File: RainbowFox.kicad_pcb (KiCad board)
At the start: 2 copper layers, 304.8 x 95.3 mm, 315 parts, among them P1 FLASH_HDR, P2 CONN_01X06, P3 USB_OTG, P4 CONN_01X04, U1 MK20DX256VLH7, U2 IS31FL3737, U3 IS31FL3737, X1 CRYSTAL_SMD

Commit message: Fixed Orientation of Keyboard-Diodes
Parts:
- turned D1 to 180 degrees
- turned D10 to 90 degrees
- turned D11 to 90 degrees
- turned D12 to 90 degrees
- turned D13 to 90 degrees
- turned D14 to 90 degrees
- turned D15 to 90 degrees
- turned D16 to 0 degrees
- turned D17 to 90 degrees
- turned D18 to 90 degrees
- turned D19 to 90 degrees
- turned D2 to 0 degrees
- turned D20 to 90 degrees
- turned D21 to 90 degrees
- turned D22 to 90 degrees
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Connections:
- D1 pad 1: Net-(D1-Pad1) -> /mcu/PTB19
- D1 pad 2: /mcu/PTB19 -> Net-(D1-Pad2)
- D10 pad 1: Net-(D10-Pad1) -> /mcu/PTB19
- D10 pad 2: /mcu/PTB19 -> Net-(D10-Pad2)
- D11 pad 1: Net-(D11-Pad1) -> /mcu/PTB19
- D11 pad 2: /mcu/PTB19 -> Net-(D11-Pad2)
- D12 pad 1: Net-(D12-Pad1) -> /mcu/PTB19
- D12 pad 2: /mcu/PTB19 -> Net-(D12-Pad2)
- D13 pad 1: Net-(D13-Pad1) -> /mcu/PTB19
- D13 pad 2: /mcu/PTB19 -> Net-(D13-Pad2)
- D14 pad 1: Net-(D14-Pad1) -> /mcu/PTB19
- D14 pad 2: /mcu/PTB19 -> Net-(D14-Pad2)
- D15 pad 1: Net-(D15-Pad1) -> /mcu/PTB19
- D15 pad 2: /mcu/PTB19 -> Net-(D15-Pad2)
- D16 pad 1: Net-(D16-Pad1) -> /mcu/PTB19
- D16 pad 2: /mcu/PTB19 -> Net-(D16-Pad2)
- D17 pad 1: Net-(D17-Pad1) -> /mcu/PTB18
- D17 pad 2: /mcu/PTB18 -> Net-(D17-Pad2)
- D18 pad 1: Net-(D18-Pad1) -> /mcu/PTB18
- D18 pad 2: /mcu/PTB18 -> Net-(D18-Pad2)
- D19 pad 1: Net-(D19-Pad1) -> /mcu/PTB18
- D19 pad 2: /mcu/PTB18 -> Net-(D19-Pad2)
- D2 pad 1: Net-(D2-Pad1) -> /mcu/PTB19
- D2 pad 2: /mcu/PTB19 -> Net-(D2-Pad2)
- D20 pad 1: Net-(D20-Pad1) -> /mcu/PTB18
- D20 pad 2: /mcu/PTB18 -> Net-(D20-Pad2)
- D21 pad 1: Net-(D21-Pad1) -> /mcu/PTB18
- D21 pad 2: /mcu/PTB18 -> Net-(D21-Pad2)
- D22 pad 1: Net-(D22-Pad1) -> /mcu/PTB18
- D22 pad 2: /mcu/PTB18 -> Net-(D22-Pad2)
- D23 pad 1: Net-(D23-Pad1) -> /mcu/PTB18
- D23 pad 2: /mcu/PTB18 -> Net-(D23-Pad2)
- D24 pad 1: Net-(D24-Pad1) -> /mcu/PTB18
- D24 pad 2: /mcu/PTB18 -> Net-(D24-Pad2)
- D25 pad 1: Net-(D25-Pad1) -> /mcu/PTB18
- D25 pad 2: /mcu/PTB18 -> Net-(D25-Pad2)
- D26 pad 1: Net-(D26-Pad1) -> /mcu/PTB18
- D26 pad 2: /mcu/PTB18 -> Net-(D26-Pad2)
- D27 pad 1: Net-(D27-Pad1) -> /mcu/PTB18
- D27 pad 2: /mcu/PTB18 -> Net-(D27-Pad2)
- D28 pad 1: Net-(D28-Pad1) -> /mcu/PTB18
- D28 pad 2: /mcu/PTB18 -> Net-(D28-Pad2)
- D29 pad 1: Net-(D29-Pad1) -> /mcu/PTB18
- D29 pad 2: /mcu/PTB18 -> Net-(D29-Pad2)
- D3 pad 1: Net-(D3-Pad1) -> /mcu/PTB19
- D3 pad 2: /mcu/PTB19 -> Net-(D3-Pad2)
- D30 pad 1: Net-(D30-Pad1) -> /mcu/PTB18
- D30 pad 2: /mcu/PTB18 -> Net-(D30-Pad2)
- D31 pad 1: Net-(D31-Pad1) -> /mcu/PTB18
- D31 pad 2: /mcu/PTB18 -> Net-(D31-Pad2)
- D32 pad 1: Net-(D32-Pad1) -> /mcu/PTC0
- D32 pad 2: /mcu/PTC0 -> Net-(D32-Pad2)
- D33 pad 1: Net-(D33-Pad1) -> /mcu/PTC0
- D33 pad 2: /mcu/PTC0 -> Net-(D33-Pad2)
- D34 pad 1: Net-(D34-Pad1) -> /mcu/PTC0
- D34 pad 2: /mcu/PTC0 -> Net-(D34-Pad2)
- D35 pad 1: Net-(D35-Pad1) -> /mcu/PTC0
- D35 pad 2: /mcu/PTC0 -> Net-(D35-Pad2)
- D36 pad 1: Net-(D36-Pad1) -> /mcu/PTC0
- D36 pad 2: /mcu/PTC0 -> Net-(D36-Pad2)
- D37 pad 1: Net-(D37-Pad1) -> /mcu/PTC0
- D37 pad 2: /mcu/PTC0 -> Net-(D37-Pad2)
- D38 pad 1: Net-(D38-Pad1) -> /mcu/PTC0
- D38 pad 2: /mcu/PTC0 -> Net-(D38-Pad2)
- D39 pad 1: Net-(D39-Pad1) -> /mcu/PTC0
- D39 pad 2: /mcu/PTC0 -> Net-(D39-Pad2)
- D4 pad 1: Net-(D4-Pad1) -> /mcu/PTB19
- D4 pad 2: /mcu/PTB19 -> Net-(D4-Pad2)
- D40 pad 1: Net-(D40-Pad1) -> /mcu/PTC0
- D40 pad 2: /mcu/PTC0 -> Net-(D40-Pad2)
- D41 pad 1: Net-(D41-Pad1) -> /mcu/PTC0
- D41 pad 2: /mcu/PTC0 -> Net-(D41-Pad2)
- D42 pad 1: Net-(D42-Pad1) -> /mcu/PTC0
- D42 pad 2: /mcu/PTC0 -> Net-(D42-Pad2)
- D43 pad 1: Net-(D43-Pad1) -> /mcu/PTC0
- D43 pad 2: /mcu/PTC0 -> Net-(D43-Pad2)
- D44 pad 1: Net-(D44-Pad1) -> /mcu/PTC0
- D44 pad 2: /mcu/PTC0 -> Net-(D44-Pad2)
- D45 pad 1: Net-(D45-Pad1) -> /mcu/PTC0
- D45 pad 2: /mcu/PTC0 -> Net-(D45-Pad2)
- D46 pad 1: Net-(D46-Pad1) -> /mcu/PTC0
- D46 pad 2: /mcu/PTC0 -> Net-(D46-Pad2)
- D47 pad 1: Net-(D47-Pad1) -> /mcu/PTB2
- D47 pad 2: /mcu/PTB2 -> Net-(D47-Pad2)
- D48 pad 1: Net-(D48-Pad1) -> /mcu/PTB2
- D48 pad 2: /mcu/PTB2 -> Net-(D48-Pad2)
- D49 pad 1: Net-(D49-Pad1) -> /mcu/PTB2
- D49 pad 2: /mcu/PTB2 -> Net-(D49-Pad2)
- D5 pad 1: Net-(D5-Pad1) -> /mcu/PTB19
- D5 pad 2: /mcu/PTB19 -> Net-(D5-Pad2)
- D50 pad 1: Net-(D50-Pad1) -> /mcu/PTB2
- D50 pad 2: /mcu/PTB2 -> Net-(D50-Pad2)
- D51 pad 1: Net-(D51-Pad1) -> /mcu/PTB2
- D51 pad 2: /mcu/PTB2 -> Net-(D51-Pad2)
- D52 pad 1: Net-(D52-Pad1) -> /mcu/PTB2
- D52 pad 2: /mcu/PTB2 -> Net-(D52-Pad2)
- D53 pad 1: Net-(D53-Pad1) -> /mcu/PTB2
- D53 pad 2: /mcu/PTB2 -> Net-(D53-Pad2)
- D54 pad 1: Net-(D54-Pad1) -> /mcu/PTB2
- D54 pad 2: /mcu/PTB2 -> Net-(D54-Pad2)
- D55 pad 1: Net-(D55-Pad1) -> /mcu/PTB2
- D55 pad 2: /mcu/PTB2 -> Net-(D55-Pad2)
- D56 pad 1: Net-(D56-Pad1) -> /mcu/PTB2
- D56 pad 2: /mcu/PTB2 -> Net-(D56-Pad2)
- D57 pad 1: Net-(D57-Pad1) -> /mcu/PTB2
- D57 pad 2: /mcu/PTB2 -> Net-(D57-Pad2)
- D58 pad 1: Net-(D58-Pad1) -> /mcu/PTB2
- D58 pad 2: /mcu/PTB2 -> Net-(D58-Pad2)
- D59 pad 1: Net-(D59-Pad1) -> /mcu/PTB2
- D59 pad 2: /mcu/PTB2 -> Net-(D59-Pad2)
- D6 pad 1: Net-(D6-Pad1) -> /mcu/PTB19
- D6 pad 2: /mcu/PTB19 -> Net-(D6-Pad2)
- D60 pad 1: Net-(D60-Pad1) -> /mcu/PTB2
- D60 pad 2: /mcu/PTB2 -> Net-(D60-Pad2)
- D61 pad 1: Net-(D61-Pad1) -> /mcu/PTB2
- D61 pad 2: /mcu/PTB2 -> Net-(D61-Pad2)
- D62 pad 1: Net-(D62-Pad1) -> /mcu/PTC10
- D62 pad 2: /mcu/PTC10 -> Net-(D62-Pad2)
- D63 pad 1: Net-(D63-Pad1) -> /mcu/PTC10
- D63 pad 2: /mcu/PTC10 -> Net-(D63-Pad2)
- D64 pad 1: Net-(D64-Pad1) -> /mcu/PTC10
- D64 pad 2: /mcu/PTC10 -> Net-(D64-Pad2)
- D65 pad 1: Net-(D65-Pad1) -> /mcu/PTC10
- D65 pad 2: /mcu/PTC10 -> Net-(D65-Pad2)
- D66 pad 1: Net-(D66-Pad1) -> /mcu/PTC10
- D66 pad 2: /mcu/PTC10 -> Net-(D66-Pad2)
- D67 pad 1: Net-(D67-Pad1) -> /mcu/PTC10
- D67 pad 2: /mcu/PTC10 -> Net-(D67-Pad2)
- D68 pad 1: Net-(D68-Pad1) -> /mcu/PTC10
- D68 pad 2: /mcu/PTC10 -> Net-(D68-Pad2)
- D69 pad 1: Net-(D69-Pad1) -> /mcu/PTC10
- D69 pad 2: /mcu/PTC10 -> Net-(D69-Pad2)
- D7 pad 1: Net-(D7-Pad1) -> /mcu/PTB19
- D7 pad 2: /mcu/PTB19 -> Net-(D7-Pad2)
- D70 pad 1: Net-(D70-Pad1) -> /mcu/PTC10
- D70 pad 2: /mcu/PTC10 -> Net-(D70-Pad2)
- D71 pad 1: Net-(D71-Pad1) -> /mcu/PTC10
- D71 pad 2: /mcu/PTC10 -> Net-(D71-Pad2)
- D8 pad 1: Net-(D8-Pad1) -> /mcu/PTB19
- D8 pad 2: /mcu/PTB19 -> Net-(D8-Pad2)
- D9 pad 1: Net-(D9-Pad1) -> /mcu/PTB19
- D9 pad 2: /mcu/PTB19 -> Net-(D9-Pad2)
- S1 pad 2: Net-(D1-Pad1) -> Net-(D1-Pad2)
- S10 pad 2: Net-(D10-Pad1) -> Net-(D10-Pad2)
- S11 pad 2: Net-(D11-Pad1) -> Net-(D11-Pad2)
- S115 pad 2: Net-(D15-Pad1) -> Net-(D15-Pad2)
- S12 pad 2: Net-(D12-Pad1) -> Net-(D12-Pad2)
- S13 pad 2: Net-(D13-Pad1) -> Net-(D13-Pad2)
- S14 pad 2: Net-(D14-Pad1) -> Net-(D14-Pad2)
- S145 pad 2: Net-(D45-Pad1) -> Net-(D45-Pad2)
- S147 pad 2: Net-(D47-Pad1) -> Net-(D47-Pad2)
- S15 pad 2: Net-(D15-Pad1) -> Net-(D15-Pad2)
- S159 pad 2: Net-(D59-Pad1) -> Net-(D59-Pad2)
- S16 pad 2: Net-(D16-Pad1) -> Net-(D16-Pad2)
- S162 pad 2: Net-(D62-Pad1) -> Net-(D62-Pad2)
- S163 pad 2: Net-(D63-Pad1) -> Net-(D63-Pad2)
- S164 pad 2: Net-(D64-Pad1) -> Net-(D64-Pad2)
- S165 pad 2: Net-(D65-Pad1) -> Net-(D65-Pad2)
- S166 pad 2: Net-(D66-Pad1) -> Net-(D66-Pad2)
- S167 pad 2: Net-(D67-Pad1) -> Net-(D67-Pad2)
- S168 pad 2: Net-(D68-Pad1) -> Net-(D68-Pad2)
- S17 pad 2: Net-(D17-Pad1) -> Net-(D17-Pad2)
- S18 pad 2: Net-(D18-Pad1) -> Net-(D18-Pad2)
- S19 pad 2: Net-(D19-Pad1) -> Net-(D19-Pad2)
- S2 pad 2: Net-(D2-Pad1) -> Net-(D2-Pad2)
- S20 pad 2: Net-(D20-Pad1) -> Net-(D20-Pad2)
- S21 pad 2: Net-(D21-Pad1) -> Net-(D21-Pad2)
- S22 pad 2: Net-(D22-Pad1) -> Net-(D22-Pad2)
- S23 pad 2: Net-(D23-Pad1) -> Net-(D23-Pad2)
- S24 pad 2: Net-(D24-Pad1) -> Net-(D24-Pad2)
- S245 pad 1: Net-(D45-Pad1) -> Net-(D45-Pad2)
- S25 pad 2: Net-(D25-Pad1) -> Net-(D25-Pad2)
- S26 pad 2: Net-(D26-Pad1) -> Net-(D26-Pad2)
- S263 pad 2: Net-(D63-Pad1) -> Net-(D63-Pad2)
- S265 pad 2: Net-(D65-Pad1) -> Net-(D65-Pad2)
- S266 pad 2: Net-(D66-Pad1) -> Net-(D66-Pad2)
- S27 pad 2: Net-(D27-Pad1) -> Net-(D27-Pad2)
- S28 pad 2: Net-(D28-Pad1) -> Net-(D28-Pad2)
- S29 pad 2: Net-(D29-Pad1) -> Net-(D29-Pad2)
- S3 pad 2: Net-(D3-Pad1) -> Net-(D3-Pad2)
- S30 pad 2: Net-(D30-Pad1) -> Net-(D30-Pad2)
- S31 pad 2: Net-(D31-Pad1) -> Net-(D31-Pad2)
- S32 pad 2: Net-(D32-Pad1) -> Net-(D32-Pad2)
- S33 pad 2: Net-(D33-Pad1) -> Net-(D33-Pad2)
- S34 pad 2: Net-(D34-Pad1) -> Net-(D34-Pad2)
- S35 pad 2: Net-(D35-Pad1) -> Net-(D35-Pad2)
- S36 pad 2: Net-(D36-Pad1) -> Net-(D36-Pad2)
- S37 pad 2: Net-(D37-Pad1) -> Net-(D37-Pad2)
- S38 pad 2: Net-(D38-Pad1) -> Net-(D38-Pad2)
- S39 pad 2: Net-(D39-Pad1) -> Net-(D39-Pad2)
- S4 pad 2: Net-(D4-Pad1) -> Net-(D4-Pad2)
- S40 pad 2: Net-(D40-Pad1) -> Net-(D40-Pad2)
- S41 pad 2: Net-(D41-Pad1) -> Net-(D41-Pad2)
- S42 pad 2: Net-(D42-Pad1) -> Net-(D42-Pad2)
- S43 pad 2: Net-(D43-Pad1) -> Net-(D43-Pad2)
- S44 pad 2: Net-(D44-Pad1) -> Net-(D44-Pad2)
- S45 pad 2: Net-(D45-Pad1) -> Net-(D45-Pad2)
- S46 pad 2: Net-(D46-Pad1) -> Net-(D46-Pad2)
- S47 pad 2: Net-(D47-Pad1) -> Net-(D47-Pad2)
- S48 pad 2: Net-(D48-Pad1) -> Net-(D48-Pad2)
- S49 pad 2: Net-(D49-Pad1) -> Net-(D49-Pad2)
- S5 pad 2: Net-(D5-Pad1) -> Net-(D5-Pad2)
- S50 pad 2: Net-(D50-Pad1) -> Net-(D50-Pad2)
- S51 pad 2: Net-(D51-Pad1) -> Net-(D51-Pad2)
- S52 pad 2: Net-(D52-Pad1) -> Net-(D52-Pad2)
- S53 pad 2: Net-(D53-Pad1) -> Net-(D53-Pad2)
- S54 pad 2: Net-(D54-Pad1) -> Net-(D54-Pad2)
- S55 pad 2: Net-(D55-Pad1) -> Net-(D55-Pad2)
- S56 pad 2: Net-(D56-Pad1) -> Net-(D56-Pad2)
- S57 pad 2: Net-(D57-Pad1) -> Net-(D57-Pad2)
- S58 pad 2: Net-(D58-Pad1) -> Net-(D58-Pad2)
- S59 pad 2: Net-(D59-Pad1) -> Net-(D59-Pad2)
- S6 pad 2: Net-(D6-Pad1) -> Net-(D6-Pad2)
- S60 pad 2: Net-(D60-Pad1) -> Net-(D60-Pad2)
- S61 pad 2: Net-(D61-Pad1) -> Net-(D61-Pad2)
- S62 pad 2: Net-(D62-Pad1) -> Net-(D62-Pad2)
- S63 pad 2: Net-(D63-Pad1) -> Net-(D63-Pad2)
- S64 pad 2: Net-(D64-Pad1) -> Net-(D64-Pad2)
- S65 pad 2: Net-(D65-Pad1) -> Net-(D65-Pad2)
- S66 pad 2: Net-(D66-Pad1) -> Net-(D66-Pad2)
- S67 pad 2: Net-(D67-Pad1) -> Net-(D67-Pad2)
- S68 pad 2: Net-(D68-Pad1) -> Net-(D68-Pad2)
- S69 pad 2: Net-(D69-Pad1) -> Net-(D69-Pad2)
- S7 pad 2: Net-(D7-Pad1) -> Net-(D7-Pad2)
- S70 pad 2: Net-(D70-Pad1) -> Net-(D70-Pad2)
- S71 pad 2: Net-(D71-Pad1) -> Net-(D71-Pad2)
- S8 pad 2: Net-(D8-Pad1) -> Net-(D8-Pad2)
- S9 pad 2: Net-(D9-Pad1) -> Net-(D9-Pad2)
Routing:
- net Net-(D45-Pad2): track 0.00 -> 53.2 mm
- net Net-(D45-Pad1): track 53.2 -> 0.00 mm
- net Net-(D67-Pad2): track 0.00 -> 33.0 mm
- net Net-(D67-Pad1): track 33.0 -> 0.00 mm
- net Net-(D65-Pad2): track 0.00 -> 26.4 mm
- net Net-(D65-Pad1): track 26.4 -> 0.00 mm
- net Net-(D68-Pad2): track 0.00 -> 23.0 mm
- net Net-(D68-Pad1): track 23.0 -> 0.00 mm
- net Net-(D15-Pad2): track 0.00 -> 22.0 mm
- net Net-(D15-Pad1): track 22.0 -> 0.00 mm
- net Net-(D66-Pad2): track 0.00 -> 21.8 mm
- net Net-(D66-Pad1): track 21.8 -> 0.00 mm
- net Net-(D47-Pad2): track 0.00 -> 18.1 mm
- net Net-(D47-Pad1): track 18.1 -> 0.00 mm
- net Net-(D59-Pad2): track 0.00 -> 16.5 mm
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
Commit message: Did some cleanup
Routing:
- net /ledmatrix/LED-A/SW11: track 326.6 -> 322.0 mm
- net /ledmatrix/IICRST: track 98.8 -> 98.0 mm
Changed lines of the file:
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@@
   (via (at 224.282 160.02) (size 0.6096) (drill 0.508) (layers Front Back) (net 21))
   (segment (start 225.056 160.794) (end 224.282 160.02) (width 0.19) (layer Back) (net 21))
-  (segment (start 190.5 147.32) (end 187.198 147.32) (width 0.19) (layer Front) (net 22))
-  (segment (start 187.198 147.32) (end 185.674 148.844) (width 0.19) (layer Front) (net 22))
+  (segment (start 190.754 147.574) (end 187.96 147.574) (width 0.19) (layer Front) (net 22))
+  (segment (start 187.96 147.574) (end 186.69 148.844) (width 0.19) (layer Front) (net 22))
   (segment (start 258.826 157.734) (end 258.826 156.718) (width 0.19) (layer Back) (net 22))
   (segment (start 248.92 145.288) (end 248.92 146.812) (width 0.19) (layer Back) (net 22))
@@
   (via (at 180.721 149.098) (size 0.6096) (drill 0.508) (layers Front Back) (net 22))
   (segment (start 180.975 148.844) (end 180.721 149.098) (width 0.19) (layer Front) (net 22))
-  (segment (start 185.674 148.844) (end 180.975 148.844) (width 0.19) (layer Front) (net 22))
+  (segment (start 186.69 148.844) (end 180.975 148.844) (width 0.19) (layer Front) (net 22))
   (segment (start 257.016 164.465) (end 254.635 164.465) (width 0.19) (layer Front) (net 22) (status 30))
   (segment (start 259.398 164.465) (end 257.016 164.465) (width 0.19) (layer Front) (net 22) (status 30))
   (segment (start 192.786 149.606) (end 219.71 149.606) (width 0.19) (layer Front) (net 22))
   (segment (start 219.71 149.606) (end 223.901 145.415) (width 0.19) (layer Front) (net 22))
-  (segment (start 192.786 149.606) (end 190.5 147.32) (width 0.19) (layer Front) (net 22))
+  (segment (start 192.786 149.606) (end 190.754 147.574) (width 0.19) (layer Front) (net 22))
   (segment (start 226.7585 153.8605) (end 227.838 154.94) (width 0.19) (layer Front) (net 23))
   (segment (start 225.9965 153.67) (end 226.187 153.8605) (width 0.19) (layer Front) (net 23))
@@
   (segment (start 207.01 90.17) (end 197.485 80.645) (width 0.19) (layer Back) (net 43) (status 20))
   (segment (start 123.484 156.448) (end 122.7295 156.448) (width 0.19) (layer Back) (net 44) (status 10))
-  (segment (start 120.968 138.874) (end 119.253 140.589) (width 0.19) (layer Back) (net 44))
-  (segment (start 119.253 140.589) (end 119.253 144.399) (width 0.19) (layer Back) (net 44))
+  (segment (start 120.968 137.795) (end 119.253 139.51) (width 0.19) (layer Back) (net 44))
+  (segment (start 119.253 139.51) (end 119.253 144.399) (width 0.19) (layer Back) (net 44))
   (segment (start 123.063 150.495) (end 122.555 151.003) (width 0.19) (layer Front) (net 44))
   (via (at 122.555 156.2735) (size 0.6096) (drill 0.508) (layers Front Back) (net 44))
   (segment (start 122.555 156.2735) (end 122.555 151.003) (width 0.19) (layer Front) (net 44))
   (via (at 123.063 150.495) (size 0.6096) (drill 0.508) (layers Front Back) (net 44))
-  (segment (start 120.968 138.874) (end 120.968 137.795) (width 0.19) (layer Back) (net 44) (status 20))
+  (segment (start 120.968 137.795) (end 120.968 137.795) (width 0.19) (layer Back) (net 44) (status 20))
   (segment (start 122.301 149.225) (end 122.301 147.447) (width 0.19) (layer Back) (net 44))
   (segment (start 122.301 147.447) (end 119.253 144.399) (width 0.19) (layer Back) (net 44))
@@
   (segment (start 159.512 81.788) (end 155.448 81.788) (width 0.19) (layer Back) (net 59))
   (segment (start 163.83 86.106) (end 159.512 81.788) (width 0.19) (layer Back) (net 59))
-  (segment (start 58.8962 156.845) (end 58.8962 156.9402) (width 0.19) (layer Back) (net 60) (status 30))
-  (segment (start 58.8962 156.9402) (end 59.944 157.988) (width 0.19) (layer Back) (net 60) (status 10))
+  (segment (start 58.8962 156.845) (end 58.8962 156.845) (width 0.19) (layer Back) (net 60) (status 30))
+  (segment (start 58.8962 156.845) (end 60.0392 157.988) (width 0.19) (layer Back) (net 60) (status 10))
   (segment (start 67.7545 157.988) (end 68.8975 156.845) (width 0.19) (layer Back) (net 60) (status 20))
-  (segment (start 59.944 157.988) (end 67.7545 157.988) (width 0.19) (layer Back) (net 60))
+  (segment (start 60.0392 157.988) (end 67.7545 157.988) (width 0.19) (layer Back) (net 60))
   (segment (start 119.38 151.384) (end 120.777 151.384) (width 0.19) (layer Back) (net 60))
   (segment (start 120.777 151.384) (end 121.539 152.146) (width 0.19) (layer Back) (net 60))
@@
   (segment (start 61.468 99.8855) (end 61.468 106.934) (width 0.19) (layer Front) (net 60) (status 10))
   (segment (start 61.2775 99.695) (end 61.468 99.8855) (width 0.19) (layer Front) (net 60) (status 30))
-  (segment (start 58.8962 156.845) (end 58.8962 153.8922) (width 0.19) (layer Back) (net 60) (status 10))
+  (segment (start 58.8962 156.845) (end 58.8962 156.845) (width 0.19) (layer Back) (net 60) (status 10))
   (segment (start 59.182 144.018) (end 59.182 138.0808) (width 0.19) (layer Back) (net 60) (status 20))
   (segment (start 57.658 145.542) (end 59.182 144.018) (width 0.19) (layer Back) (net 60))
-  (segment (start 57.658 152.654) (end 57.658 145.542) (width 0.19) (layer Back) (net 60))
-  (segment (start 58.8962 153.8922) (end 57.658 152.654) (width 0.19) (layer Back) (net 60))
+  (segment (start 57.658 155.6068) (end 57.658 145.542) (width 0.19) (layer Back) (net 60))
+  (segment (start 58.8962 156.845) (end 57.658 155.6068) (width 0.19) (layer Back) (net 60))
   (segment (start 59.182 138.0808) (end 58.8962 137.795) (width 0.19) (layer Back) (net 60) (status 30))
   (segment (start 147.002 118.745) (end 147.002 110.426) (width 0.19) (layer Back) (net 60) (status 10))
@@
   (segment (start 142.24 82.296) (end 134.366 82.296) (width 0.19) (layer Back) (net 60))
   (segment (start 134.366 82.296) (end 132.715 80.645) (width 0.19) (layer Back) (net 60) (status 20))
+  (segment (start 66.5162 137.795) (end 66.5162 139.4778) (width 0.19) (layer Back) (net 61))
+  (segment (start 66.5162 139.4778) (end 66.548 139.446) (width 0.19) (layer Back) (net 61))
   (segment (start 119.888 151.003) (end 121.031 151.003) (width 0.19) (layer Back) (net 61))
   (segment (start 121.031 151.003) (end 121.666 151.638) (width 0.19) (layer Back) (net 61))
@@
   (segment (start 69.342 136.3821) (end 69.596 136.6361) (width 0.19) (layer Back) (net 61))
   (segment (start 65.532 143.764) (end 65.532 140.462) (width 0.19) (layer Back) (net 61))
+  (segment (start 64.77 144.526) (end 65.532 143.764) (width 0.19) (layer Back) (net 61))
+  (segment (start 64.77 146.304) (end 64.77 144.526) (width 0.19) (layer Back) (net 61))
+  (segment (start 66.5162 148.0502) (end 64.77 146.304) (width 0.19) (layer Back) (net 61))
+  (segment (start 66.5162 156.845) (end 66.5162 148.0502) (width 0.19) (layer Back) (net 61) (status 10))
   (segment (start 65.532 140.462) (end 66.548 139.446) (width 0.19) (layer Back) (net 61))
   (segment (start 66.548 139.446) (end 68.453 139.446) (width 0.19) (layer Back) (net 61))
+  (segment (start 69.596 138.303) (end 69.596 136.6361) (width 0.19) (layer Back) (net 61))
   (segment (start 68.453 139.446) (end 69.596 138.303) (width 0.19) (layer Back) (net 61))
-  (segment (start 69.596 138.303) (end 69.596 136.6361) (width 0.19) (layer Back) (net 61))
   (segment (start 69.596 136.6361) (end 74.8823 136.6361) (width 0.19) (layer Back) (net 61))
   (segment (start 74.8823 136.6361) (end 76.0412 137.795) (width 0.19) (layer Back) (net 61) (status 20))
@@
   (segment (start 68.80225 99.59975) (end 67.7545 98.552) (width 0.19) (layer Front) (net 61) (status 10))
   (segment (start 70.1358 117.602) (end 71.2788 118.745) (width 0.19) (layer Front) (net 61) (status 20))
-  (segment (start 66.5162 156.845) (end 66.5162 148.0502) (width 0.19) (layer Back) (net 61) (status 10))
-  (segment (start 66.5162 148.0502) (end 64.77 146.304) (width 0.19) (layer Back) (net 61))
-  (segment (start 64.77 146.304) (end 64.77 144.526) (width 0.19) (layer Back) (net 61))
-  (segment (start 64.77 144.526) (end 65.532 143.764) (width 0.19) (layer Back) (net 61))
-  (segment (start 65.532 143.764) (end 65.532 138.7792) (width 0.19) (layer Back) (net 61))
-  (segment (start 65.532 138.7792) (end 66.5162 137.795) (width 0.19) (layer Back) (net 61) (status 20))
   (segment (start 149.86 99.695) (end 149.86 100.838) (width 0.19) (layer Back) (net 61) (status 10))
   (segment (start 148.082 112.205) (end 154.622 118.745) (width 0.19) (layer Back) (net 61) (status 20))
@@
   (segment (start 200.406 159.766) (end 200.406 157.226) (width 0.19) (layer Back) (net 65))
   (via (at 200.406 159.766) (size 0.6096) (drill 0.508) (layers Front Back) (net 65))
-  (segment (start 200.406 165.354) (end 200.406 159.766) (width 0.19) (layer Front) (net 65))
-  (segment (start 167.894 169.037) (end 196.723 169.037) (width 0.19) (layer Front) (net 65))
+  (segment (start 200.406 164.084) (end 200.406 159.766) (width 0.19) (layer Front) (net 65))
+  (segment (start 167.894 169.037) (end 195.453 169.037) (width 0.19) (layer Front) (net 65))
   (segment (start 166.37 167.513) (end 167.894 169.037) (width 0.19) (layer Front) (net 65))
   (segment (start 148.082 167.513) (end 166.37 167.513) (width 0.19) (layer Front) (net 65))
-  (segment (start 200.406 165.354) (end 196.723 169.037) (width 0.19) (layer Front) (net 65))
+  (segment (start 200.406 164.084) (end 195.453 169.037) (width 0.19) (layer Front) (net 65))
   (segment (start 137.795 158.115) (end 133.223 158.115) (width 0.19) (layer Front) (net 66))
   (segment (start 124.984 157.948) (end 124.984 159.782) (width 0.19) (layer Back) (net 66) (status 10))

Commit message: Switched to different Debug Ports
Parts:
- removed W1, W2: TEST_1P, Measurement_Points:Measurement_Point_Round-SMD-Pad_Small
- added P5: CONN_01X02, lib.pretty:Conn-2, B.Cu at (154.4, 164.8)
- added P6: CONN_01X04, lib.pretty:Conn-4, B.Cu at (163.1, 156.7)
- P2: footprint Pin_Headers:Pin_Header_Straight_1x06_Pitch2.00mm -> lib.pretty:Conn-6
- P4: footprint Pin_Headers:Pin_Header_Straight_1x04_Pitch2.00mm -> lib.pretty:Conn-4
- moved ? 37.4 mm to (199.4, 167.4) (x2)
- moved ? 6.10 mm to (150.9, 148.6)
- moved P2 5.00 mm to (229.1, 162.2), turned to 270 degrees
- moved P4 3.00 mm to (70.3, 87.6), turned to 0 degrees
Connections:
- S147 pad 1: /mcu/PTE1 -> /mcu/PTD6
- S163 pad 1: /mcu/PTE1 -> /mcu/PTD6
- S164 pad 1: /mcu/PTE2 -> /mcu/PTD5
- S17 pad 1: /mcu/PTE1 -> /mcu/PTD6
- S18 pad 1: /mcu/PTE2 -> /mcu/PTD5
- S2 pad 1: /mcu/PTE1 -> /mcu/PTD6
- S263 pad 1: /mcu/PTE1 -> /mcu/PTD6
- S3 pad 1: /mcu/PTE2 -> /mcu/PTD5
- S32 pad 1: /mcu/PTE1 -> /mcu/PTD6
- S33 pad 1: /mcu/PTE2 -> /mcu/PTD5
- S47 pad 1: /mcu/PTE1 -> /mcu/PTD6
- S48 pad 1: /mcu/PTE2 -> /mcu/PTD5
- S63 pad 1: /mcu/PTE1 -> /mcu/PTD6
- S64 pad 1: /mcu/PTE2 -> /mcu/PTD5
- U1 pad 1: /mcu/PTE1 -> /mcu/RX1
- U1 pad 2: /mcu/PTE2 -> /mcu/TX1
- U1 pad 62: (no net) -> /mcu/PTD5
- U1 pad 63: (no net) -> /mcu/PTD6
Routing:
- net /mcu/PTD5: track 0.00 -> 298.6 mm, vias 0 -> 1
- net /mcu/PTE2: track 297.6 -> 0.00 mm
- net /mcu/PTD6: track 0.00 -> 279.4 mm, vias 0 -> 1
- net /mcu/PTE1: track 277.1 -> 0.00 mm, vias 1 -> 0
- net /mcu/TX1: track 0.00 -> 18.8 mm
- net /mcu/RX1: track 0.00 -> 18.7 mm
- net /ledmatrix/INTB: track 32.5 -> 47.8 mm
- net +3V3: track 179.9 -> 173.7 mm
- net GND: track 344.3 -> 347.0 mm
- net /mcu/PTC4: track 159.3 -> 160.7 mm
- net /mcu/PTC5: track 248.9 -> 249.8 mm
- net /mcu/PTC3: track 268.6 -> 267.9 mm
- net /mcu/PTC2: track 306.7 -> 305.9 mm
- net /mcu/PTC1: track 295.7 -> 295.0 mm
- net /mcu/PTC0: track 337.7 -> 337.0 mm
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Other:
- board text added: "INTB"
- board text added: "RX1"
- board text added: "SDB"
- board text added: "TX1"

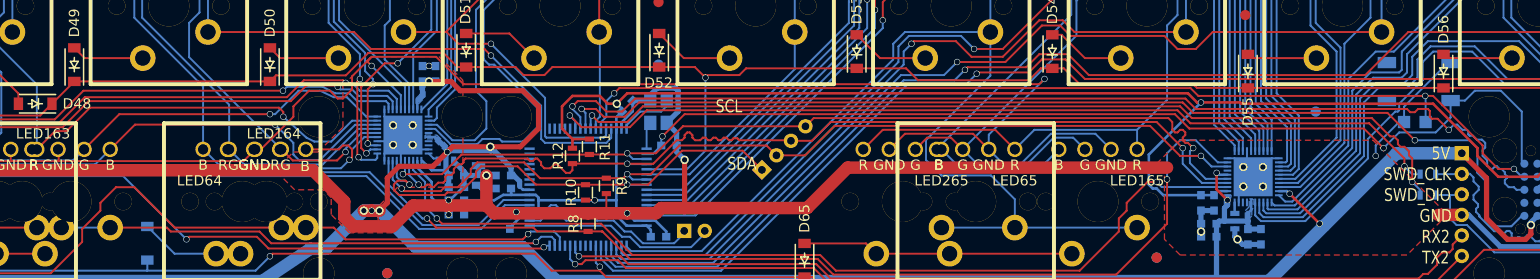
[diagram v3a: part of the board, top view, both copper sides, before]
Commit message: Addressed the Points raised in Issue #2
Added Resistor to ground for firmware-LED
Connect VBAT to 3.3V
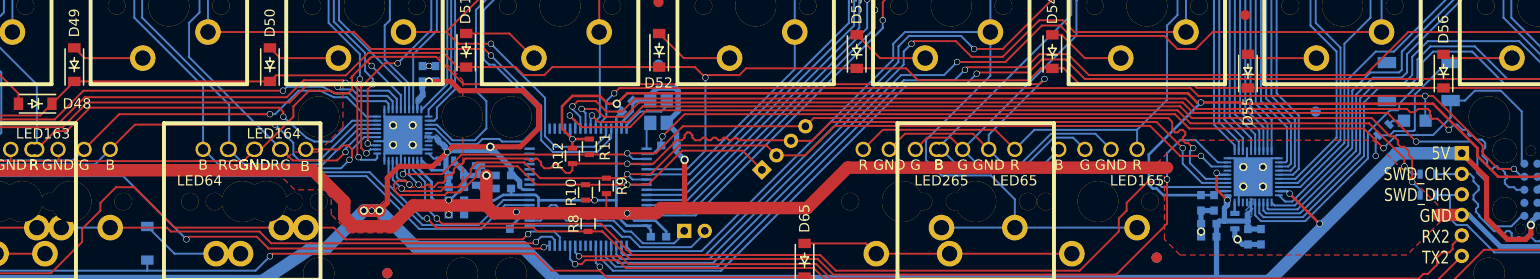
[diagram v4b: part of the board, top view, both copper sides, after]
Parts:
- added R13: 1k, Resistors_SMD:R_0603, B.Cu at (221.5, 154.9)
- moved LED72 0.13 mm to (224.5, 154.1)
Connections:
- LED72 pad 1: GND -> Net-(LED72-Pad1)
- U1 pad 21: (no net) -> +3V3
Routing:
- net GND: track 347.0 -> 348.6 mm
- net Net-(LED72-Pad1): track 0.00 -> 1.62 mm
- net +3V3: track 173.7 -> 174.8 mm, vias 4 -> 5
- net /mcu/PTA13: track 115.1 -> 115.9 mm
- net /mcu/PTA12: track 112.6 -> 113.3 mm
